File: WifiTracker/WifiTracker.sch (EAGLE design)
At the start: 15 parts, among them Y1 16MHz

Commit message: WifiTracker v1 schematic done
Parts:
- added 5V_REG, U1: V_REG_317DPACK, SparkFun-IC-Power:V_REG_317DPACK
- added POWER: (no value), pinhead:PINHD-1X2
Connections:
- new net VIN: 5V_REG.IN
- net 3VCC: now also U1.OUT
- net 5VCC: now also 5V_REG.OUT, POWER.1, U1.IN
- net GND: now also 5V_REG.ADJ, POWER.2, U1.ADJ
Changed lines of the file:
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@@
 <part name="S1" library="SparkFun-Switches" library_urn="urn:adsk.eagle:library:535" deviceset="MOMENTARY-SWITCH-SPST" device="-PTH-6.0MM" package3d_urn="urn:adsk.eagle:package:40163/1"/>
 <part name="C3" library="SparkFun-Capacitors" library_urn="urn:adsk.eagle:library:510" deviceset="0.1UF" device="-0603-25V-(+80/-20%)" package3d_urn="urn:adsk.eagle:package:37414/1" value="0.1uF"/>
+<part name="5V_REG" library="SparkFun-IC-Power" library_urn="urn:adsk.eagle:library:526" deviceset="V_REG_317" device="DPACK" package3d_urn="urn:adsk.eagle:package:39071/1"/>
+<part name="U1" library="SparkFun-IC-Power" library_urn="urn:adsk.eagle:library:526" deviceset="V_REG_317" device="DPACK" package3d_urn="urn:adsk.eagle:package:39071/1"/>
+<part name="POWER" library="pinhead" library_urn="urn:adsk.eagle:library:325" deviceset="PINHD-1X2" device="" package3d_urn="urn:adsk.eagle:package:22435/2"/>
 </parts>
 <sheets>
@@
 <attribute name="NAME" x="-31.496" y="43.561" size="1.778" layer="95" font="vector"/>
 <attribute name="VALUE" x="-31.496" y="38.481" size="1.778" layer="96" font="vector"/>
+</instance>
+<instance part="5V_REG" gate="G$1" x="109.22" y="12.7" smashed="yes">
+<attribute name="NAME" x="111.76" y="5.08" size="1.778" layer="95"/>
+<attribute name="VALUE" x="111.76" y="2.54" size="1.778" layer="96"/>
+</instance>
+<instance part="U1" gate="G$1" x="129.54" y="45.72" smashed="yes">
+<attribute name="NAME" x="132.08" y="38.1" size="1.778" layer="95"/>
+<attribute name="VALUE" x="132.08" y="35.56" size="1.778" layer="96"/>
+</instance>
+<instance part="POWER" gate="G$1" x="147.32" y="-10.16" smashed="yes">
+<attribute name="NAME" x="140.97" y="-4.445" size="1.778" layer="95"/>
+<attribute name="VALUE" x="140.97" y="-15.24" size="1.778" layer="96"/>
 </instance>
 </instances>
@@
 <label x="-40.64" y="38.1" size="1.778" layer="95" rot="R180" xref="yes"/>
 </segment>
+<segment>
+<pinref part="5V_REG" gate="G$1" pin="ADJ"/>
+<wire x1="109.22" y1="5.08" x2="109.22" y2="-2.54" width="0.1524" layer="91"/>
+<label x="109.22" y="-2.54" size="1.778" layer="95" rot="R270" xref="yes"/>
+<pinref part="POWER" gate="G$1" pin="2"/>
+<wire x1="144.78" y1="-10.16" x2="111.76" y2="-10.16" width="0.1524" layer="91"/>
+<wire x1="111.76" y1="-10.16" x2="111.76" y2="5.08" width="0.1524" layer="91"/>
+<wire x1="111.76" y1="5.08" x2="109.22" y2="5.08" width="0.1524" layer="91"/>
+<junction x="109.22" y="5.08"/>
+</segment>
+<segment>
+<pinref part="U1" gate="G$1" pin="ADJ"/>
+<wire x1="129.54" y1="38.1" x2="129.54" y2="30.48" width="0.1524" layer="91"/>
+<label x="129.54" y="30.48" size="1.778" layer="95" rot="R270" xref="yes"/>
+</segment>
 </net>
 <net name="3VCC" class="0">
@@
 <junction x="111.76" y="73.66"/>
 <junction x="111.76" y="71.12"/>
+</segment>
+<segment>
+<pinref part="U1" gate="G$1" pin="OUT"/>
+<wire x1="137.16" y1="45.72" x2="144.78" y2="45.72" width="0.1524" layer="91"/>
+<label x="144.78" y="45.72" size="1.778" layer="95" xref="yes"/>
 </segment>
 </net>
@@
 <label x="-40.64" y="45.72" size="1.778" layer="95" rot="R180" xref="yes"/>
 </segment>
+<segment>
+<pinref part="5V_REG" gate="G$1" pin="OUT"/>
+<wire x1="116.84" y1="12.7" x2="124.46" y2="12.7" width="0.1524" layer="91"/>
+<label x="124.46" y="12.7" size="1.778" layer="95" xref="yes"/>
+<wire x1="116.84" y1="12.7" x2="116.84" y2="45.72" width="0.1524" layer="91"/>
+<junction x="116.84" y="12.7"/>
+<pinref part="U1" gate="G$1" pin="IN"/>
+<wire x1="116.84" y1="45.72" x2="121.92" y2="45.72" width="0.1524" layer="91"/>
+<pinref part="POWER" gate="G$1" pin="1"/>
+<wire x1="116.84" y1="12.7" x2="116.84" y2="-7.62" width="0.1524" layer="91"/>
+<wire x1="116.84" y1="-7.62" x2="144.78" y2="-7.62" width="0.1524" layer="91"/>
+</segment>
 </net>
 <net name="STA_TXD" class="0">
@@
 </segment>
 </net>
+<net name="VIN" class="0">
+<segment>
+<pinref part="5V_REG" gate="G$1" pin="IN"/>
+<wire x1="101.6" y1="12.7" x2="93.98" y2="12.7" width="0.1524" layer="91"/>
+<label x="93.98" y="12.7" size="1.778" layer="95" rot="R180" xref="yes"/>
+</segment>
+</net>

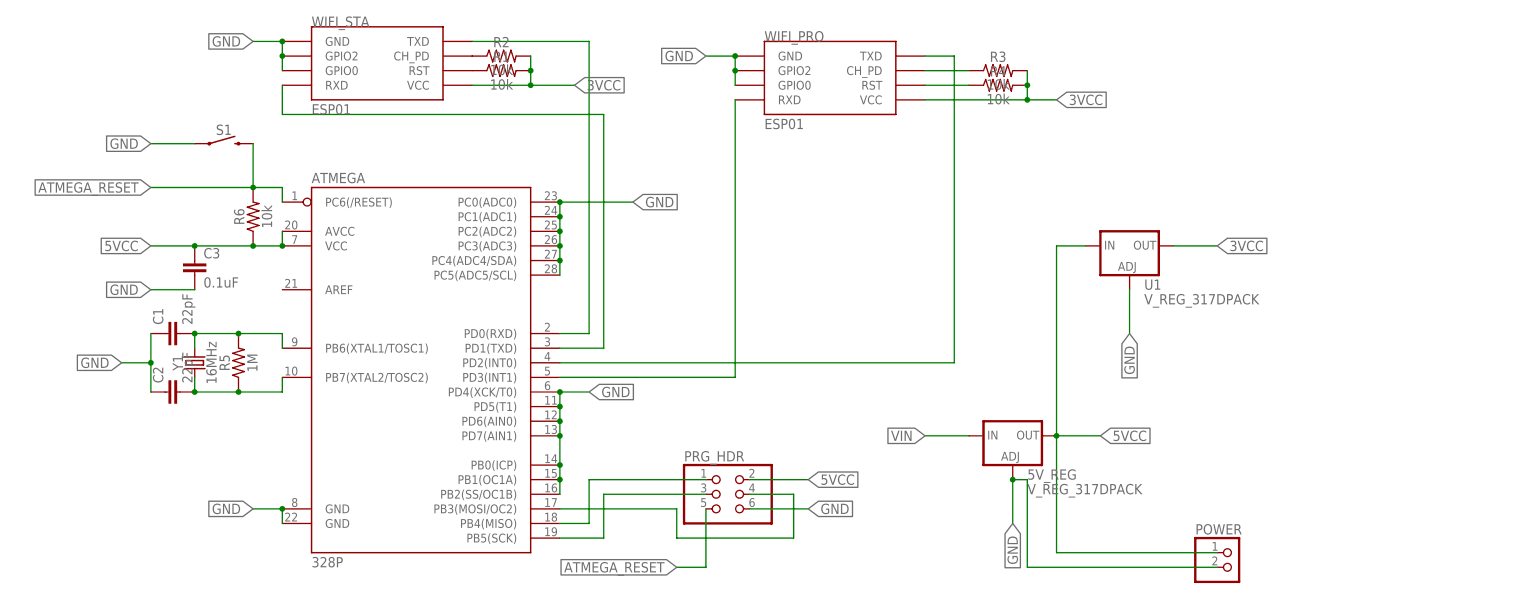
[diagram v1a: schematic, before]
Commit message: Schematic done
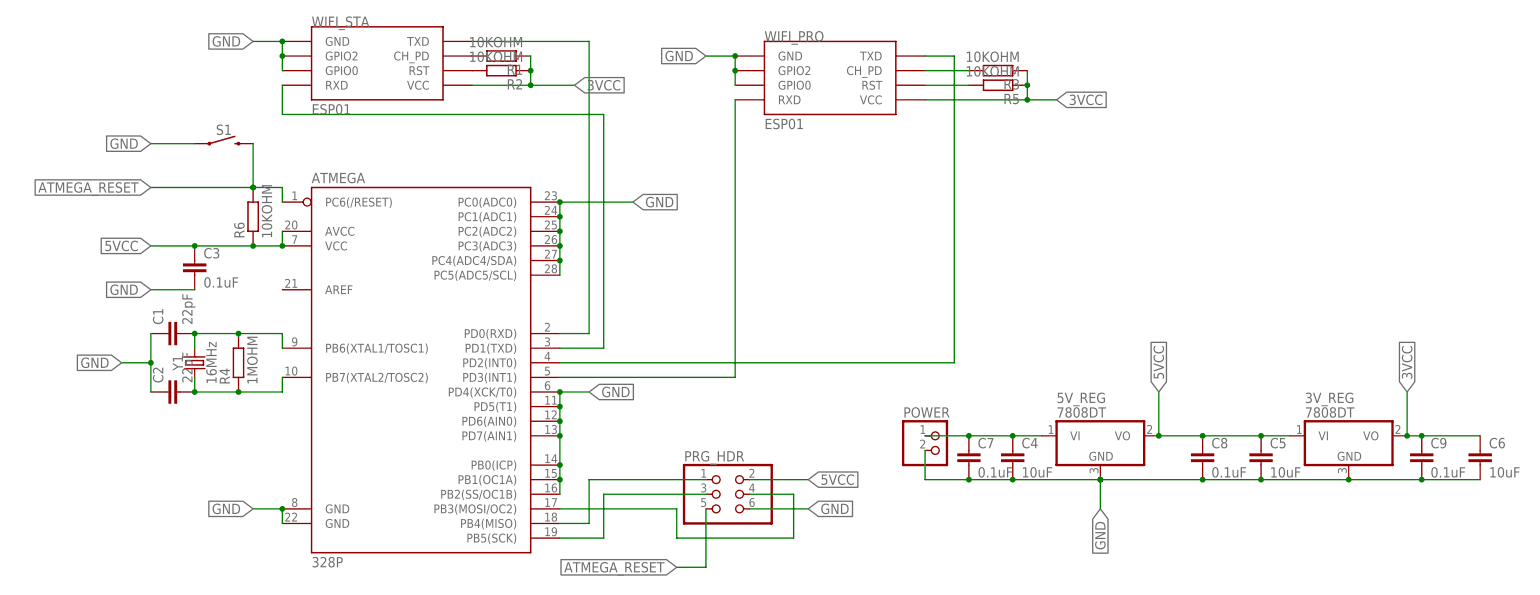
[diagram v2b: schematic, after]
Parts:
- removed U1: V_REG_317DPACK, SparkFun-IC-Power:V_REG_317DPACK
- added 3V_REG: 7808DT, linear:7808DT
- added C4, C5, C6: 10uF, SparkFun-Capacitors:1.0UF-1206-50V-10%
- added C7, C8, C9: 0.1uF, SparkFun-Capacitors:1.0UF-1206-50V-10%
- 5V_REG: value V_REG_317DPACK -> 7808DT; device SparkFun-IC-Power:V_REG_317DPACK -> linear:7808DT
- C1, C2: device SparkFun-Capacitors:22PF-0603-50V-5% -> SparkFun-Capacitors:1.0UF-1206-50V-10%
- C3: device SparkFun-Capacitors:0.1UF-0603-25V-(+80/-20%) -> SparkFun-Capacitors:1.0UF-1206-50V-10%
- R1, R2, R3, R6: value 10k -> 10KOHM; device SparkFun-Resistors:10KOHM-0603-1/10W-1% -> eagle-ltspice:RR1210
- R4: value 10k -> 1MOHM; device SparkFun-Resistors:10KOHM-0603-1/10W-1% -> eagle-ltspice:RR1210
- R5: value 1M -> 10KOHM; device SparkFun-Resistors:1MOHM-0603-1/4W-5% -> eagle-ltspice:RR1210
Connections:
- net 3VCC: now also 3V_REG.VO, C6.1, C9.1, R1.1, R2.1, R3.1, R5.1; no longer R1.2, R2.2, R3.2, R4.2, U1.OUT
- net 5VCC: now also 3V_REG.VI, 5V_REG.VO, C5.1, C8.1; no longer 5V_REG.OUT, POWER.1, U1.IN
- net GND: now also 3V_REG.GND, 5V_REG.GND, C4.2, C5.2, C6.2, C7.2, C8.2, C9.2; no longer 5V_REG.ADJ, U1.ADJ
- net N$1: now also R1.2, WIFI_STA.CH_PD; no longer R1.1, WIFI_STA.RST
- net N$2: now also R2.2, WIFI_STA.RST; no longer R2.1, WIFI_STA.CH_PD
- net N$3: now also R3.2; no longer R3.1
- net N$4: now also R5.2; no longer R4.1
- net VIN: now also 5V_REG.VI, C4.1, C7.1, POWER.1; no longer 5V_REG.IN
- net XTAL1: now also R4.2; no longer R5.2
- net XTAL2: now also R4.1; no longer R5.1
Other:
- moved on the sheet: POWER

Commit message: Rev 1
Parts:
- removed C3: 0.1uF, SparkFun-Capacitors:1.0UF-1206-50V-10%
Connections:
- net N$1 renamed STA_CH_PD
- net N$2 renamed STA_RST
- net N$3 renamed PRO_CH_PD
- net N$4 renamed PRO_RST
- net 5VCC: no longer C3.1
- net GND: no longer C3.2
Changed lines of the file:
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@@
 <?xml version="1.0" encoding="utf-8"?>
 <!DOCTYPE eagle SYSTEM "eagle.dtd">
-<eagle version="9.3.1">
+<eagle version="9.3.0">
 <drawing>
 <settings>
@@
 <part name="R2" library="eagle-ltspice" library_urn="urn:adsk.eagle:library:217" deviceset="R" device="R1210" package3d_urn="urn:adsk.eagle:package:13299/1" value="10KOHM"/>
 <part name="R3" library="eagle-ltspice" library_urn="urn:adsk.eagle:library:217" deviceset="R" device="R1210" package3d_urn="urn:adsk.eagle:package:13299/1" value="10KOHM"/>
-<part name="C3" library="SparkFun-Capacitors" library_urn="urn:adsk.eagle:library:510" deviceset="1.0UF" device="-1206-50V-10%" package3d_urn="urn:adsk.eagle:package:37426/1" value="0.1uF"/>
 <part name="C1" library="SparkFun-Capacitors" library_urn="urn:adsk.eagle:library:510" deviceset="1.0UF" device="-1206-50V-10%" package3d_urn="urn:adsk.eagle:package:37426/1" value="22pF"/>
 <part name="C2" library="SparkFun-Capacitors" library_urn="urn:adsk.eagle:library:510" deviceset="1.0UF" device="-1206-50V-10%" package3d_urn="urn:adsk.eagle:package:37426/1" value="22pF"/>
@@
 <attribute name="NAME" x="110.49" y="74.7014" size="1.778" layer="95" rot="R180"/>
 <attribute name="VALUE" x="110.49" y="79.502" size="1.778" layer="96" rot="R180"/>
-</instance>
-<instance part="C3" gate="G$1" x="-33.02" y="40.64" smashed="yes">
-<attribute name="NAME" x="-31.496" y="43.561" size="1.778" layer="95" font="vector"/>
-<attribute name="VALUE" x="-31.496" y="38.481" size="1.778" layer="96" font="vector"/>
 </instance>
 <instance part="C1" gate="G$1" x="-35.56" y="30.48" smashed="yes" rot="R90">
@@
 <junction x="30.48" y="20.32"/>
 <label x="35.56" y="20.32" size="1.778" layer="95" xref="yes"/>
-</segment>
-<segment>
-<wire x1="-33.02" y1="38.1" x2="-40.64" y2="38.1" width="0.1524" layer="91"/>
-<label x="-40.64" y="38.1" size="1.778" layer="95" rot="R180" xref="yes"/>
-<pinref part="C3" gate="G$1" pin="2"/>
 </segment>
 <segment>
@@
 <junction x="-17.78" y="45.72"/>
 <wire x1="-17.78" y1="45.72" x2="-22.86" y2="45.72" width="0.1524" layer="91"/>
-<wire x1="-22.86" y1="45.72" x2="-33.02" y2="45.72" width="0.1524" layer="91"/>
+<wire x1="-22.86" y1="45.72" x2="-40.64" y2="45.72" width="0.1524" layer="91"/>
 <label x="-40.64" y="45.72" size="1.778" layer="95" rot="R180" xref="yes"/>
 <pinref part="R6" gate="G$1" pin="1"/>
 <junction x="-22.86" y="45.72"/>
-<pinref part="C3" gate="G$1" pin="1"/>
-<wire x1="-33.02" y1="45.72" x2="-40.64" y2="45.72" width="0.1524" layer="91"/>
-<junction x="-33.02" y="45.72"/>
 </segment>
 <segment>
@@
 </segment>
 </net>
-<net name="N$3" class="0">
+<net name="PRO_CH_PD" class="0">
 <segment>
 <pinref part="WIFI_PRO" gate="G$1" pin="CH_PD"/>
@@
 </segment>
 </net>
-<net name="N$4" class="0">
+<net name="PRO_RST" class="0">
 <segment>
 <pinref part="WIFI_PRO" gate="G$1" pin="RST"/>
@@
 </segment>
 </net>
-<net name="N$1" class="0">
+<net name="STA_CH_PD" class="0">
 <segment>
 <pinref part="R1" gate="G$1" pin="2"/>
@@
 </segment>
 </net>
-<net name="N$2" class="0">
+<net name="STA_RST" class="0">
 <segment>
 <pinref part="R2" gate="G$1" pin="2"/>
@@
 </sheet>
 </sheets>
+<errors>
+</errors>
 </schematic>
 </drawing>
